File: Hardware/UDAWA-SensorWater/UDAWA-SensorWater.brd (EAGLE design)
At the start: 160 x 100 mm, 9 parts

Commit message: Routing PCB #6
Routing PCB
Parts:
- moved TDS 36.9 mm to (76.2, 7.62)
- moved ARDUINO_NANO1 16.6 mm to (74.9, 53.3), turned to 90 degrees
- moved R4 14.2 mm to (67.3, 21.6), turned to 180 degrees
- moved DS18B20 2.54 mm to (55.9, 8.89), turned to 180 degrees
- moved U$1 2.54 mm to (26.7, 49.5)
- moved R3 1.80 mm to (53.3, 21.6)
- turned U$2 to 0 degrees
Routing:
- net 5V: track 22.5 -> 174.1 mm, vias 0 -> 2
- net GND: track 41.9 -> 188.1 mm
- net HV1: track 0.00 -> 74.8 mm, vias 0 -> 2
- net HV2: track 0.00 -> 74.6 mm
- net 3V3: track 0.00 -> 62.4 mm
- net D2: track 0.00 -> 53.0 mm
- net LV2: track 0.00 -> 46.6 mm
- net A2: track 0.00 -> 44.1 mm
- net A0: track 0.00 -> 41.6 mm
- net LV1: track 0.00 -> 37.9 mm
- net A1: track 0.00 -> 33.9 mm

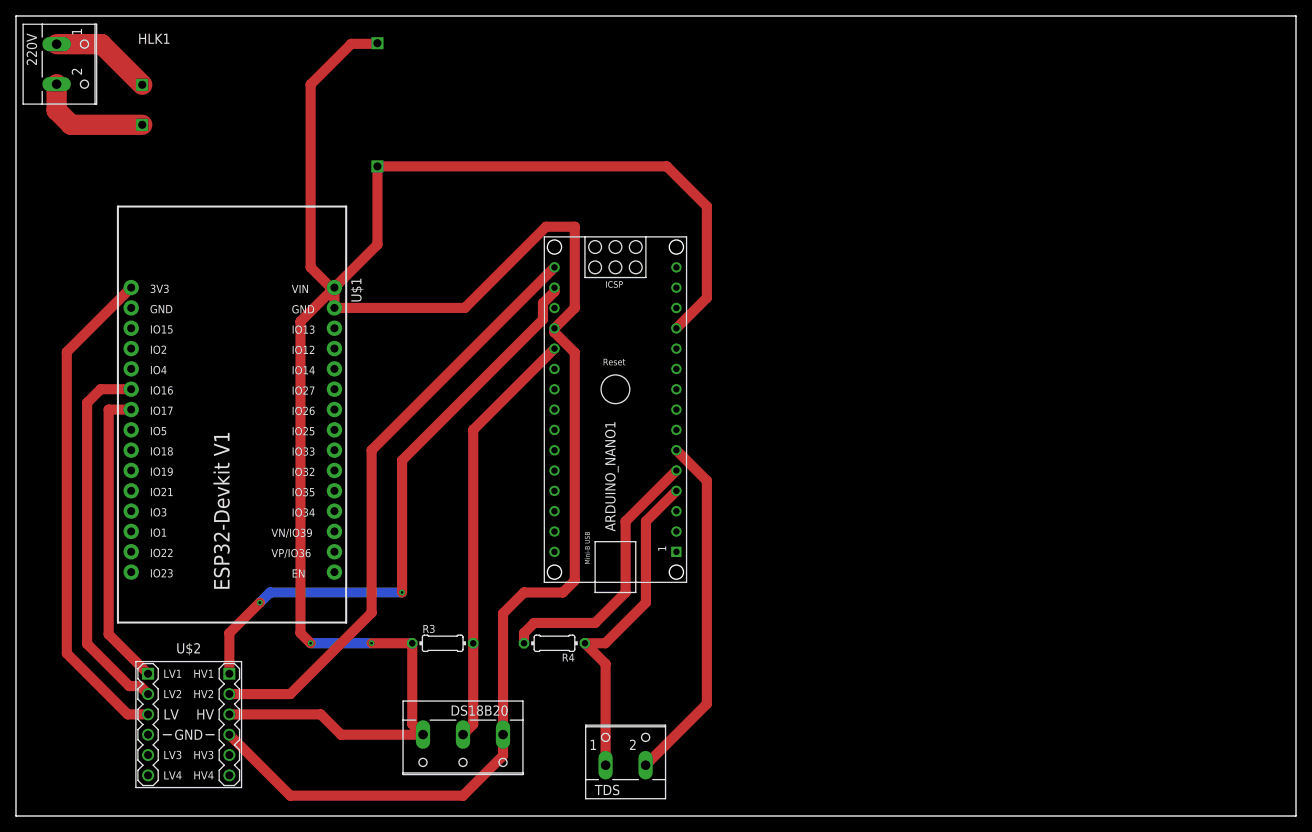
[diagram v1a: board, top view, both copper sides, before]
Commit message: Revert "Merge pull request #16 from NarinLab/sensor-water"
This reverts commit fa909a87a465dd37d6351bcf5a105db5a344029a, reversing
changes made to da9ed59faa8e6d8399543247dba95a3195e07114.

Conflict Error Fix
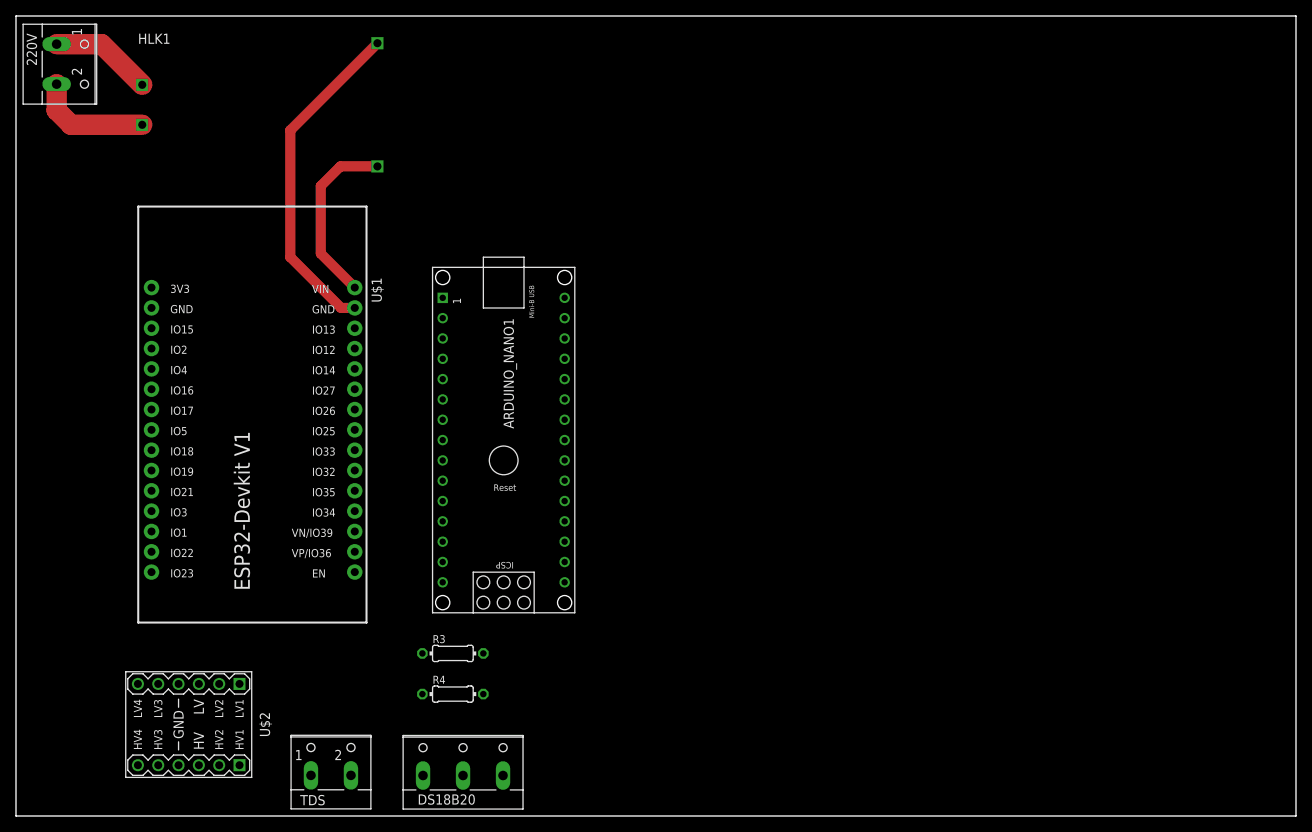
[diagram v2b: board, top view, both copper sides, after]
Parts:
- moved TDS 36.9 mm to (39.4, 6.35)
- moved ARDUINO_NANO1 16.6 mm to (61.0, 44.5), turned to 270 degrees
- moved R4 14.2 mm to (54.6, 15.2), turned to 0 degrees
- moved DS18B20 2.54 mm to (55.9, 6.35), turned to 0 degrees
- moved U$1 2.54 mm to (29.2, 49.5)
- moved R3 1.80 mm to (54.6, 20.3)
- turned U$2 to 270 degrees
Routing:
- net 5V: track 174.1 -> 22.5 mm, vias 2 -> 0
- net GND: track 188.1 -> 41.9 mm
- net HV1: track 74.8 -> 0.00 mm, vias 2 -> 0
- net HV2: track 74.6 -> 0.00 mm
- net 3V3: track 62.4 -> 0.00 mm
- net D2: track 53.0 -> 0.00 mm
- net LV2: track 46.6 -> 0.00 mm
- net A2: track 44.1 -> 0.00 mm
- net A0: track 41.6 -> 0.00 mm
- net LV1: track 37.9 -> 0.00 mm
- net A1: track 33.9 -> 0.00 mm
